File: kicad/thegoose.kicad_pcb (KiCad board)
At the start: 4 copper layers, 73.4 x 43 mm, 120 parts, among them J1 USB_C_Receptacle_USB2.0_16P, J12 LED stick, J3 XT30PW-M, J4 USB-A host, J5 IO 3x6 RA, Q1 AO4407A, SW1 Power, SW2 BOOT, U1 DRV8251A, U10 RP2354A, U11 SRV05-4, U14 74AHCT1G125, U15 DRV8251A, U16 DRV8251A, U17 DRV8251A, U2 DRV8251A, U3 DRV8251A, U4 AP64500SP-13, U6 SRV05-4, U8 HT7550-1, U9 XC6206P332MR, Y1 12MHz

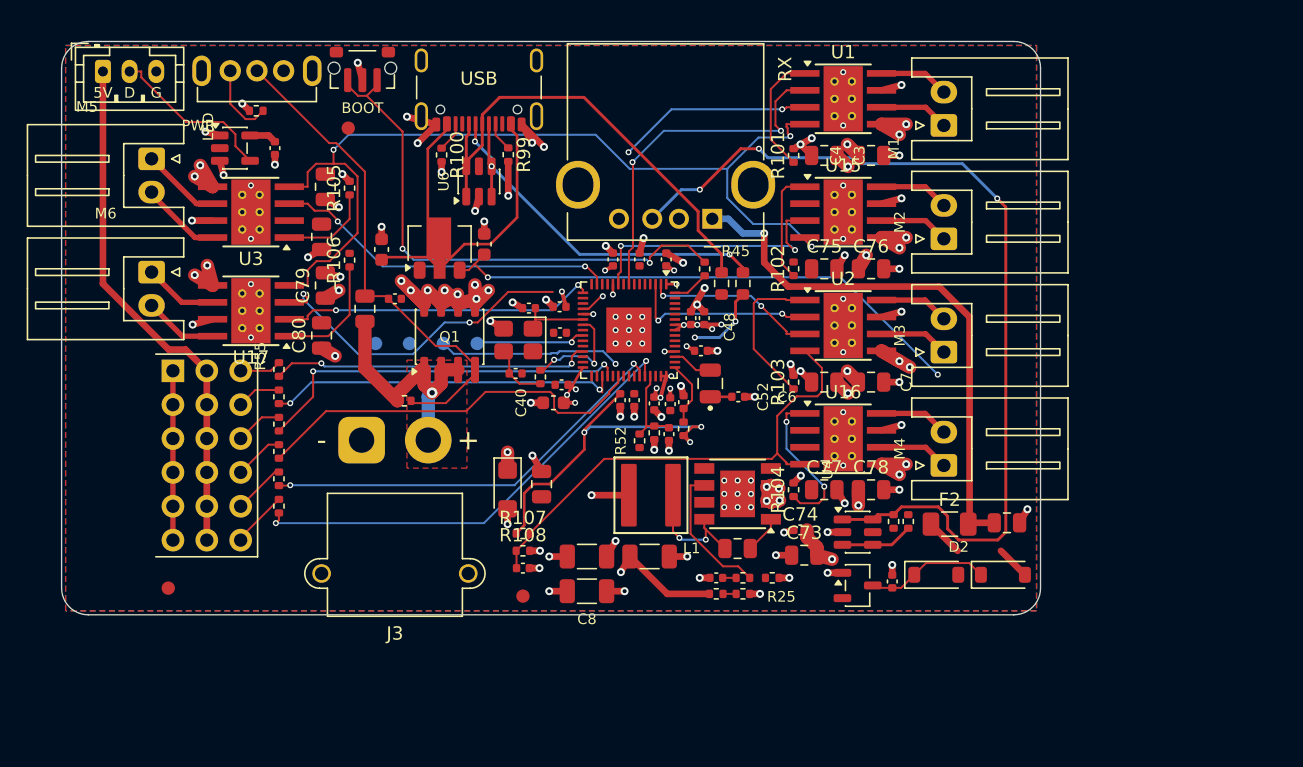
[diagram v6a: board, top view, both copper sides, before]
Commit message: Place the brain double-sided at 66.3 x 34 mm, unrouted
- tools/place_double.py rebuilds the placement from scratch: parts on both
  sides, M1-M6 swapped to JST PH S2B-PH-K (C173752), J3 under J4, the
  switches in the bottom-right corner, the USB-C ESD and series resistors
  on the front between J1 and U10.
- Pulls in the 2026-10-20 schematic change (IO5/IO6 off the ADC pins,
  R109/R114 15k USB-A pull-downs).
- Reassigns U10 GPIOs for the new layout, keeping each motor on its own
  PWM slice and IO4-IO6 on slices 1 and 4; USB-A moves to GPIO26/27.
- Adds back-side fiducials FID4-FID6.
- The old partial autoroute is kept in kicad/reference/.

Co-Authored-By: Claude Opus 5.5 <noreply@anthropic.com>
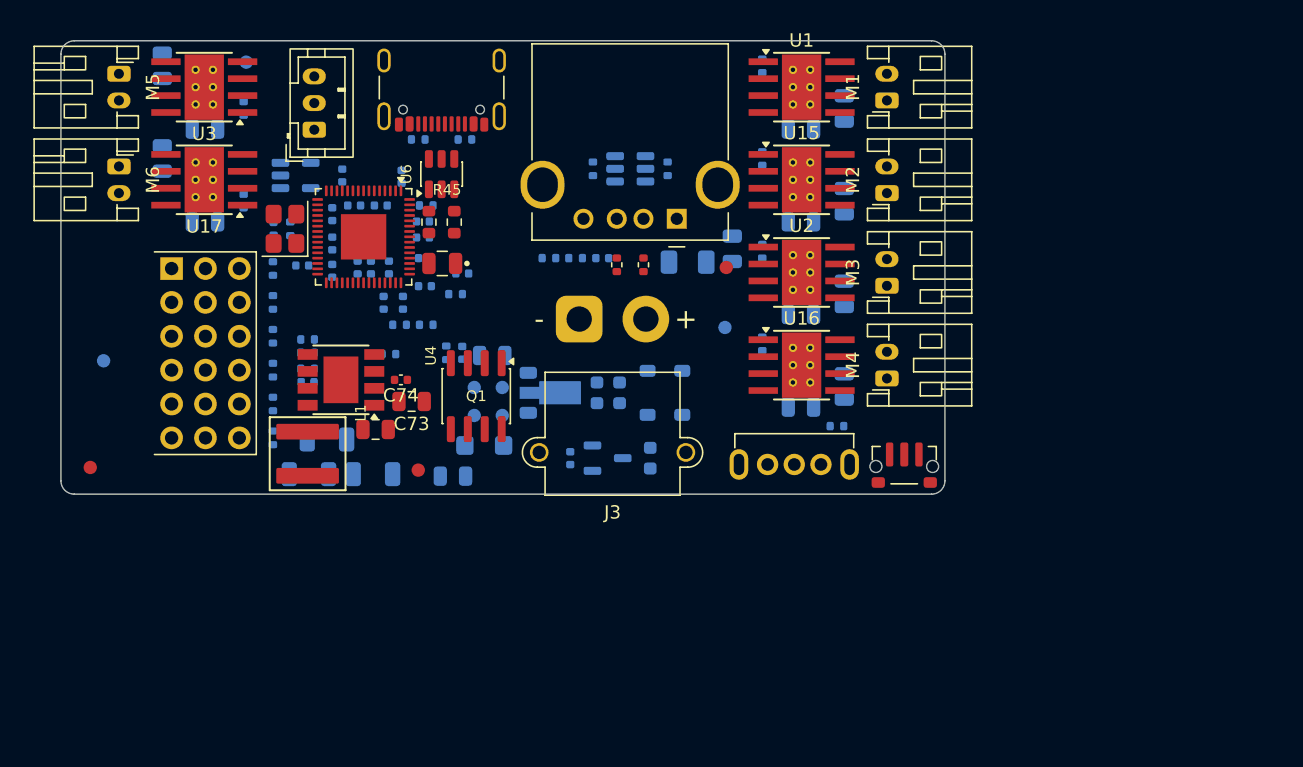
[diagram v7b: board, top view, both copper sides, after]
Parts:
- added FID4: Fiducial, Fiducial:Fiducial_1mm_Mask2mm, B.Cu at (103.2, 124.0)
- added FID5: Fiducial, Fiducial:Fiducial_1mm_Mask2mm, B.Cu at (149.8, 121.5)
- added FID6: Fiducial, Fiducial:Fiducial_1mm_Mask2mm, B.Cu at (113.8, 101.5)
- added R109: 15k, Resistor_SMD:R_0402_1005Metric, B.Cu at (139.8, 109.5)
- added R114: 15k, Resistor_SMD:R_0402_1005Metric, B.Cu at (145.4, 109.5)
- C10, C11, C12, C15, C16, C3, C37, C38, C39, C4, C40, C41, C42, C43, C44, C45, C46, C47, C48, C49, C5, C50, C51, C52, C53, C54, C55, C56, C57, C59, C6, C61, C69, C7, C71, C72, C75, C76, C77, C78, C79, C8, C80, C81, D2, D3, D4, F2, R100, R101, R102, R103, R104, R105, R106, R107, R108, R25, R26, R27, R28, R40, R41, R42, R43, R46, R52, R53, R55, R56, R57, R58, R59, R60, R99, U11, U14, U8, U9: moved to B.Cu
- M1, M2, M3, M4, M5, M6: footprint Connector_JST:JST_XH_S2B-XH-A_1x02_P2.50mm_Horizontal -> Connector_JST:JST_PH_S2B-PH-K_1x02_P2.00mm_Horizontal
- moved SW2 50.4 mm to (163.2, 131.9), turned to 0 degrees
- moved SW1 50.0 mm to (154.9, 131.7), turned to 180 degrees
- moved R41 49.6 mm to (158.2, 128.8), turned to 0 degrees
- moved R27 37.3 mm to (118.5, 123.3), turned to 0 degrees
- moved R28 36.2 mm to (118.5, 124.5)
- moved R26 36.1 mm to (118.5, 122.3), turned to 0 degrees
- moved C16 34.0 mm to (118.5, 125.5)
- moved R25 33.3 mm to (124.5, 123.5), turned to 0 degrees
- moved U11 32.1 mm to (142.7, 109.5)
- moved C74 32.0 mm to (125.5, 125.4), turned to 180 degrees
- moved C73 31.6 mm to (126.2, 127.0), turned to 180 degrees
- moved U4 31.0 mm to (121.0, 125.4)
- moved C59 29.1 mm to (150.3, 115.5), turned to 90 degrees
- moved FID2 29.0 mm to (149.8, 117.0)
- moved C14 28.6 mm to (123.5, 129.1)
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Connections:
- U1 pad 2: GPIO5_M1B -> GPIO11_M1B
- U1 pad 3: GPIO4_M1A -> GPIO10_M1A
- U10 pad 10: GPIO7_M2A -> LED_DIN
- U10 pad 14: GPIO10_M5A -> GPIO10_M1A
- U10 pad 15: GPIO11_M5B -> GPIO11_M1B
- U10 pad 16: GPIO12_M6B -> GPIO12_M5A
- U10 pad 17: GPIO13_M6A -> GPIO13_M5B
- U10 pad 18: GPIO14_M4A -> GPIO14_M6A
- U10 pad 19: GPIO15_M4B -> GPIO15_M6B
- U10 pad 2: GPIO0_M3A -> GPIO0_M2A
- U10 pad 28: unconnected-(U10-GPIO17-Pad28) -> IO2_GPIO
- U10 pad 29: LED_DIN -> IO3_GPIO
- U10 pad 3: GPIO1_M3B -> GPIO1_M2B
- U10 pad 31: unconnected-(U10-GPIO19-Pad31) -> IO4_GPIO
- U10 pad 32: unconnected-(U10-GPIO20-Pad32) -> GPIO20_M4A
- U10 pad 33: IO2_GPIO -> GPIO21_M4B
- U10 pad 34: IO3_GPIO -> GPIO22_M3A
- U10 pad 35: unconnected-(U10-GPIO23-Pad35) -> GPIO23_M3B
- U10 pad 36: IO4_GPIO -> IO5_GPIO
- U10 pad 37: unconnected-(U10-GPIO25-Pad37) -> IO6_GPIO
- U10 pad 4: /MCU & USB/USBA_GPIO_P -> unconnected-(U10-GPIO2-Pad4)
- U10 pad 40: IO5_GPIO -> /MCU & USB/USBA_GPIO_N
- U10 pad 41: IO6_GPIO -> /MCU & USB/USBA_GPIO_P
- U10 pad 5: /MCU & USB/USBA_GPIO_N -> unconnected-(U10-GPIO3-Pad5)
- U10 pad 7: GPIO4_M1A -> unconnected-(U10-GPIO4-Pad7)
- U10 pad 8: GPIO5_M1B -> unconnected-(U10-GPIO5-Pad8)
- U10 pad 9: GPIO6_M2B -> unconnected-(U10-GPIO6-Pad9)
- U15 pad 2: GPIO6_M2B -> GPIO1_M2B
- U15 pad 3: GPIO7_M2A -> GPIO0_M2A
- U16 pad 2: GPIO15_M4B -> GPIO21_M4B
- U16 pad 3: GPIO14_M4A -> GPIO20_M4A
- U17 pad 2: GPIO12_M6B -> GPIO15_M6B
- U17 pad 3: GPIO13_M6A -> GPIO14_M6A
- U2 pad 2: GPIO1_M3B -> GPIO23_M3B
- U2 pad 3: GPIO0_M3A -> GPIO22_M3A
- U3 pad 2: GPIO11_M5B -> GPIO13_M5B
- U3 pad 3: GPIO10_M5A -> GPIO12_M5A
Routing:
- net /Motor drivers/MOT_VREF: track 106.8 -> 0.00 mm, vias 3 -> 0
- net GND: track 91.0 -> 0.00 mm, vias 98 -> 0
- net /MCU & USB/USBA_P: track 69.4 -> 0.00 mm, vias 3 -> 0
- net VCC: track 60.5 -> 0.00 mm, vias 4 -> 0
- net VSYS: track 52.1 -> 0.00 mm, vias 34 -> 0
- net +3V3: track 45.2 -> 0.00 mm, vias 22 -> 0
- net Net-(J4-VBUS): track 41.1 -> 0.00 mm, vias 1 -> 0
- net Net-(R46-Pad2): track 40.6 -> 0.00 mm, vias 2 -> 0
- net Net-(D2-A): track 40.5 -> 0.00 mm, vias 2 -> 0
- net Net-(Q1-G): track 37.4 -> 0.00 mm
- net USB_P: track 35.5 -> 0.00 mm
- net IO6_GPIO: track 34.8 -> 0.00 mm, vias 2 -> 0
- net IO5_GPIO: track 31.6 -> 0.00 mm, vias 2 -> 0
- net USB_N: track 31.6 -> 0.00 mm, vias 3 -> 0
- net VBUS: track 30.7 -> 0.00 mm
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- removed copper zone on In2.Cu, net +3V3
- removed copper zone on B.Cu, net GND
- removed copper zone on F.Cu, net GND
- removed copper zone on In1.Cu, net GND
- removed copper zone on In2.Cu, net GND
- removed copper zone on F.Cu, net PACK+
- removed copper zone on In2.Cu, net VCC
- removed copper zone on In2.Cu, net VSYS
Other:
- board size 73.4 x 43 mm -> 66.3 x 34 mm
- board text removed: "+"
- board text removed: "-"
- board text removed: "5V"
- board text removed: "BOOT"
- board text removed: "D"
- board text removed: "G"
- board text removed: "J5 IO S1 (top) ... S6 (bottom), recessed: pin tips 1 mm inside the left wall's outer face; keep x 0-4.5 clear for the plugs"
- board text removed: "LED"
- board text removed: "LED STICK ZONE 51 x 10 mm on the inside of the top wall (z about 8-18 mm, above the USB ports): keep the pack clear"
- board text removed: "PWR"
- board text removed: "RX"
- board text removed: "SWD / RUN / GND pads TP1-TP4 (bottom): SWCLK, SWDIO, RUN, GND at 2.54 mm, TP1 nearest U10 (east end)"
- board text removed: "USB"

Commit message: Rotate U10 to 0 deg and re-place the brain at 66.6 x 32 mm, unrouted
USB now runs straight down from J1 into U10's north pins; IO goes west to J5,
which moves to the top of the left wall with M5/M6 below it. SW1 sits under
U16 and SW2 in the bottom-right corner; Q1 is east of J3. GPIO map redone for
the new orientation (IO1-6 on GPIO0-3/8/9, motors on GPIO12-17/20-23/26-27,
USB-A on GPIO24/25, LED on GPIO29). ERC clean, DRC parity clean.

Co-Authored-By: Claude Opus 5.5 <noreply@anthropic.com>
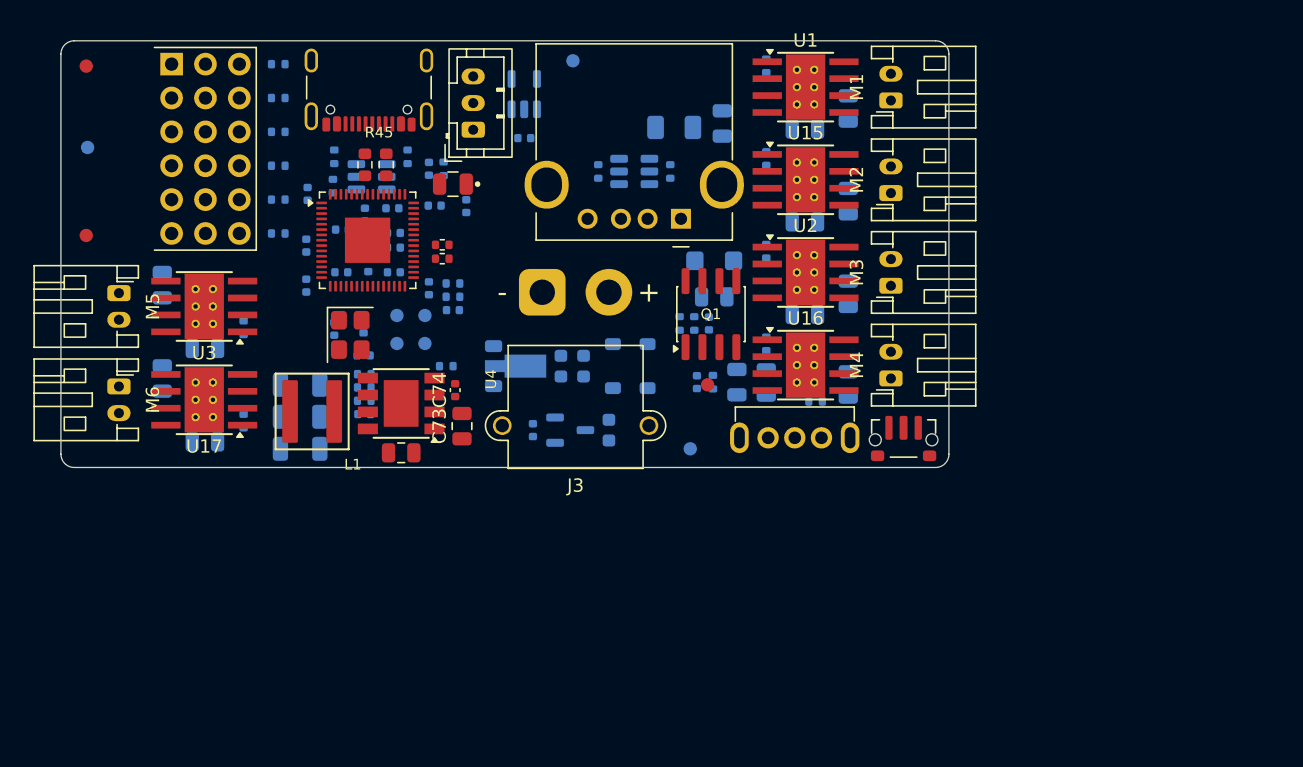
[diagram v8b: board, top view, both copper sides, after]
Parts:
- U6: moved to B.Cu
- moved FID2 48.1 mm to (101.8, 114.5)
- moved FID1 30.1 mm to (101.8, 101.8)
- moved FID6 24.5 mm to (138.3, 101.5)
- moved C15 23.8 mm to (148.9, 119.2)
- moved FID3 22.6 mm to (148.4, 125.8)
- moved D4 22.1 mm to (148.9, 116.5)
- moved R40 20.1 mm to (148.8, 125.5)
- moved Q1 18.6 mm to (148.7, 120.5), turned to 90 degrees
- moved C72 18.5 mm to (150.7, 125.5), turned to 90 degrees
- moved U14 18.2 mm to (134.7, 104.0), turned to 90 degrees
- moved C71 17.7 mm to (147.7, 125.5)
- moved C79 16.5 mm to (110.8, 130.0)
- moved C80 16.5 mm to (107.5, 125.3)
- moved M6 16.5 mm to (104.3, 125.9)
- moved R106 16.5 mm to (113.7, 128.5)
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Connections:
- U1 pad 2: GPIO11_M1B -> GPIO27_M1B
- U1 pad 3: GPIO10_M1A -> GPIO26_M1A
- U10 pad 10: LED_DIN -> unconnected-(U10-GPIO7-Pad10)
- U10 pad 12: unconnected-(U10-GPIO8-Pad12) -> IO5_GPIO
- U10 pad 13: unconnected-(U10-GPIO9-Pad13) -> IO6_GPIO
- U10 pad 14: GPIO10_M1A -> unconnected-(U10-GPIO10-Pad14)
- U10 pad 15: GPIO11_M1B -> unconnected-(U10-GPIO11-Pad15)
- U10 pad 2: GPIO0_M2A -> IO1_GPIO
- U10 pad 27: IO1_GPIO -> GPIO16_M4A
- U10 pad 28: IO2_GPIO -> GPIO17_M4B
- U10 pad 29: IO3_GPIO -> unconnected-(U10-GPIO18-Pad29)
- U10 pad 3: GPIO1_M2B -> IO2_GPIO
- U10 pad 31: IO4_GPIO -> unconnected-(U10-GPIO19-Pad31)
- U10 pad 32: GPIO20_M4A -> GPIO20_M3A
- U10 pad 33: GPIO21_M4B -> GPIO21_M3B
- U10 pad 34: GPIO22_M3A -> GPIO22_M2A
- U10 pad 35: GPIO23_M3B -> GPIO23_M2B
- U10 pad 36: IO5_GPIO -> /MCU & USB/USBA_GPIO_N
- U10 pad 37: IO6_GPIO -> /MCU & USB/USBA_GPIO_P
- U10 pad 4: unconnected-(U10-GPIO2-Pad4) -> IO3_GPIO
- U10 pad 40: /MCU & USB/USBA_GPIO_N -> GPIO26_M1A
- U10 pad 41: /MCU & USB/USBA_GPIO_P -> GPIO27_M1B
- U10 pad 43: unconnected-(U10-GPIO29/ADC3-Pad43) -> LED_DIN
- U10 pad 5: unconnected-(U10-GPIO3-Pad5) -> IO4_GPIO
- U15 pad 2: GPIO1_M2B -> GPIO23_M2B
- U15 pad 3: GPIO0_M2A -> GPIO22_M2A
- U16 pad 2: GPIO21_M4B -> GPIO17_M4B
- U16 pad 3: GPIO20_M4A -> GPIO16_M4A
- U2 pad 2: GPIO23_M3B -> GPIO21_M3B
- U2 pad 3: GPIO22_M3A -> GPIO20_M3A
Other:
- board size 66.3 x 34 mm -> 66.6 x 32 mm
